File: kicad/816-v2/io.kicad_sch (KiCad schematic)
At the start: 11 parts, among them J2 UART, J3 VIA1 Connector, J4 VIA2 Connector, U10 W65C22NxP, U11 W65C51NxP, U9 W65C22NxP, Y2 1.8342MHz

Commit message: Update KiCad files to get ready for PCB design
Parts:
- removed J3: VIA1 Connector, Connector_PinHeader_2.54mm:PinHeader_2x12_P2.54mm_Vertical, symbol Connector:Conn_01x24_Pin
- added D3, D4: SD103A, Diode_THT:D_DO-35_SOD27_P7.62mm_Horizontal, symbol Device:D_Schottky
- added J10: Mini-DIN-6, custom:TE_5749180-1, symbol Connector:Mini-DIN-6
- added J3: VIA1 Port B, Connector_PinHeader_2.54mm:PinHeader_2x06_P2.54mm_Vertical, symbol Connector:Conn_01x12_Pin
- added J5: PATA, Connector_IDC:IDC-Header_2x20_P2.54mm_Vertical, symbol Connector_Generic:Conn_02x20_Odd_Even
- added J6: PATA_PWR, Connector_PinHeader_2.54mm:PinHeader_1x02_P2.54mm_Vertical, symbol Connector:Conn_01x02_Pin
- added R6, R7: 10K, Resistor_THT:R_Axial_DIN0207_L6.3mm_D2.5mm_P7.62mm_Horizontal, symbol Device:R
- added U6: ATtiny26L-8P, Package_DIP:DIP-20_W7.62mm_Socket, symbol MCU_Microchip_ATtiny:ATtiny26L-8P
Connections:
- net A0: now also J5.35 (Pin_35)
- net A1: now also J5.33 (Pin_33)
- net A2: now also J5.36 (Pin_36)
- net D0: now also J5.17 (Pin_17)
- net D1: now also J5.15 (Pin_15)
- net D2: now also J5.13 (Pin_13)
- net D3: now also J5.11 (Pin_11)
- net D4: now also J5.9 (Pin_9)
- net D5: now also J5.7 (Pin_7)
- net D6: now also J5.5 (Pin_5)
- net D7: now also J5.3 (Pin_3)
- net GND: now also J10.3, J3.10 (Pin_10), J5.19 (Pin_19), J5.2 (Pin_2), J5.22 (Pin_22), J5.24 (Pin_24), J5.26 (Pin_26), J5.30 (Pin_30), J5.40 (Pin_40), J6.2 (Pin_2), U6.16 (GND), U6.6 (GND)
- net RESB: now also J5.1 (Pin_1), U6.10 (~{RESET}/PB7)
- net VCC: now also J10.4, J3.1 (Pin_1), J5.38 (Pin_38), J6.1 (Pin_1), U6.15 (AVCC), U6.5 (VCC)
- net CA1: now reaches U9.40 (CA1)
- net CA1: now also U6.8 (XTAL2/PB5)
- net CA2: now reaches U9.39 (CA2)
- net CA2: now also U6.9 (PB6)
- net at U9.10 (PB0): now also J3.2 (Pin_2)
- net at U9.11 (PB1): now also J3.3 (Pin_3)
- net at U9.12 (PB2): now also J3.4 (Pin_4)
- net at U9.13 (PB3): now also J3.5 (Pin_5)
- net at U9.14 (PB4): now also J3.6 (Pin_6)
- net at U9.15 (PB5): now also J3.7 (Pin_7)
- net at U9.16 (PB6): now also J3.8 (Pin_8)
- net PA0: now reaches U9.2 (PA0)
- net PA0: now also U6.20 (PA0)
- net at U9.17 (PB7): now also J3.9 (Pin_9)
- net at U9.18 (CB1): now also J3.11 (Pin_11)
- net at U9.19 (CB2): now also J3.12 (Pin_12)
- net PA1: now reaches U9.3 (PA1)
- net PA1: now also U6.19 (PA1)
- net PA2: now reaches U9.4 (PA2)
- net PA2: now also U6.18 (PA2)
- net PA3: now reaches U9.5 (PA3)
- net PA3: now also U6.17 (AREF/PA3)
- net PA4: now reaches U9.6 (PA4)
- net PA4: now also U6.14 (PA4)
- net PA5: now reaches U9.7 (PA5)
- net PA5: now also U6.13 (PA5)
- net PA6: now reaches U9.8 (PA6)
- net PA6: now also U6.12 (PA6)
- net PA7: now reaches U9.9 (PA7)
- net PA7: now also U6.11 (PA7)
- net IRQ1: no longer names the net of U9.21 (~{IRQ})
- net IRQ1: now also D4.1 (K)
- net IRQ2: no longer names the net of U10.21 (~{IRQ})
- net IRQ2: now also D3.1 (K)
- new net: J10.5, R6.1
- new net: J10.1, R7.1
- new net IO5CS: J5.37 (Pin_37)
- new net IRQB: D3.2 (A), D4.2 (A)
- new net OE: J5.25 (Pin_25)
- new net PS2CLK: R6.2, U6.4 (PB3)
- new net PS2DATA: R7.2, U6.7 (XTAL1/PB4)
- new net WE: J5.23 (Pin_23)
- no-connect marks 9 -> 31
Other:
- moved on the sheet: RN3

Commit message: Update KiCad files
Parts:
- removed RN3: 10k, Resistor_THT:R_Array_SIP8, symbol Device:R_Network07
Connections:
- net VCC: now also U10.24 (CS1), U11.2 (CS1), U9.24 (CS1)
- net IRQ3: no longer names the net of U11.26 (~{IRQ})
- no-connect marks 31 -> 29

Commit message: Update KiCad files new pcb revision, hopefully working
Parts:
- added C10: 0.1uF, Capacitor_THT:C_Disc_D4.3mm_W1.9mm_P5.00mm, symbol Device:C
- J2: symbol Connector:Conn_01x04_Pin -> Connector_Generic:Conn_01x04
- J3: symbol Connector:Conn_01x12_Pin -> Connector_Generic:Conn_01x12
- J4: symbol Connector:Conn_01x24_Pin -> Connector_Generic:Conn_01x24
- J6: symbol Connector:Conn_01x02_Pin -> Connector_Generic:Conn_01x02
- U10, U9: value W65C22NxP -> W65C22S; symbol PCM_65xx-library:W65C22NxP -> custom:W65C22S
- U11: value W65C51NxP -> W65C51
- U6: value ATtiny26L-8P -> ATtiny26L
- Y2: footprint Package_DIP:DIP-8_W7.62mm_Socket -> Oscillator:Oscillator_DIP-8
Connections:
- net GND: now also C10.2
- net PS2CLK: now also J10.5
- net PS2DATA: now also J10.1
- net VCC: now also R6.1, R7.1, C10.1
- net IO1CS renamed ~{IO1CS}
- net IO2CS renamed ~{IO2CS}
- net IO3CS renamed ~{IO3CS}
- net IO5CS renamed ~{IO5CS}
- net IRQB renamed ~{IRQ}
- net OE renamed ~{OE}
- net RESB renamed ~{RES}
- net RWB renamed R/~{W}
- net WE renamed ~{WE}
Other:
- moved on the sheet: C1, C5, C6, D3, D4, J10, U6

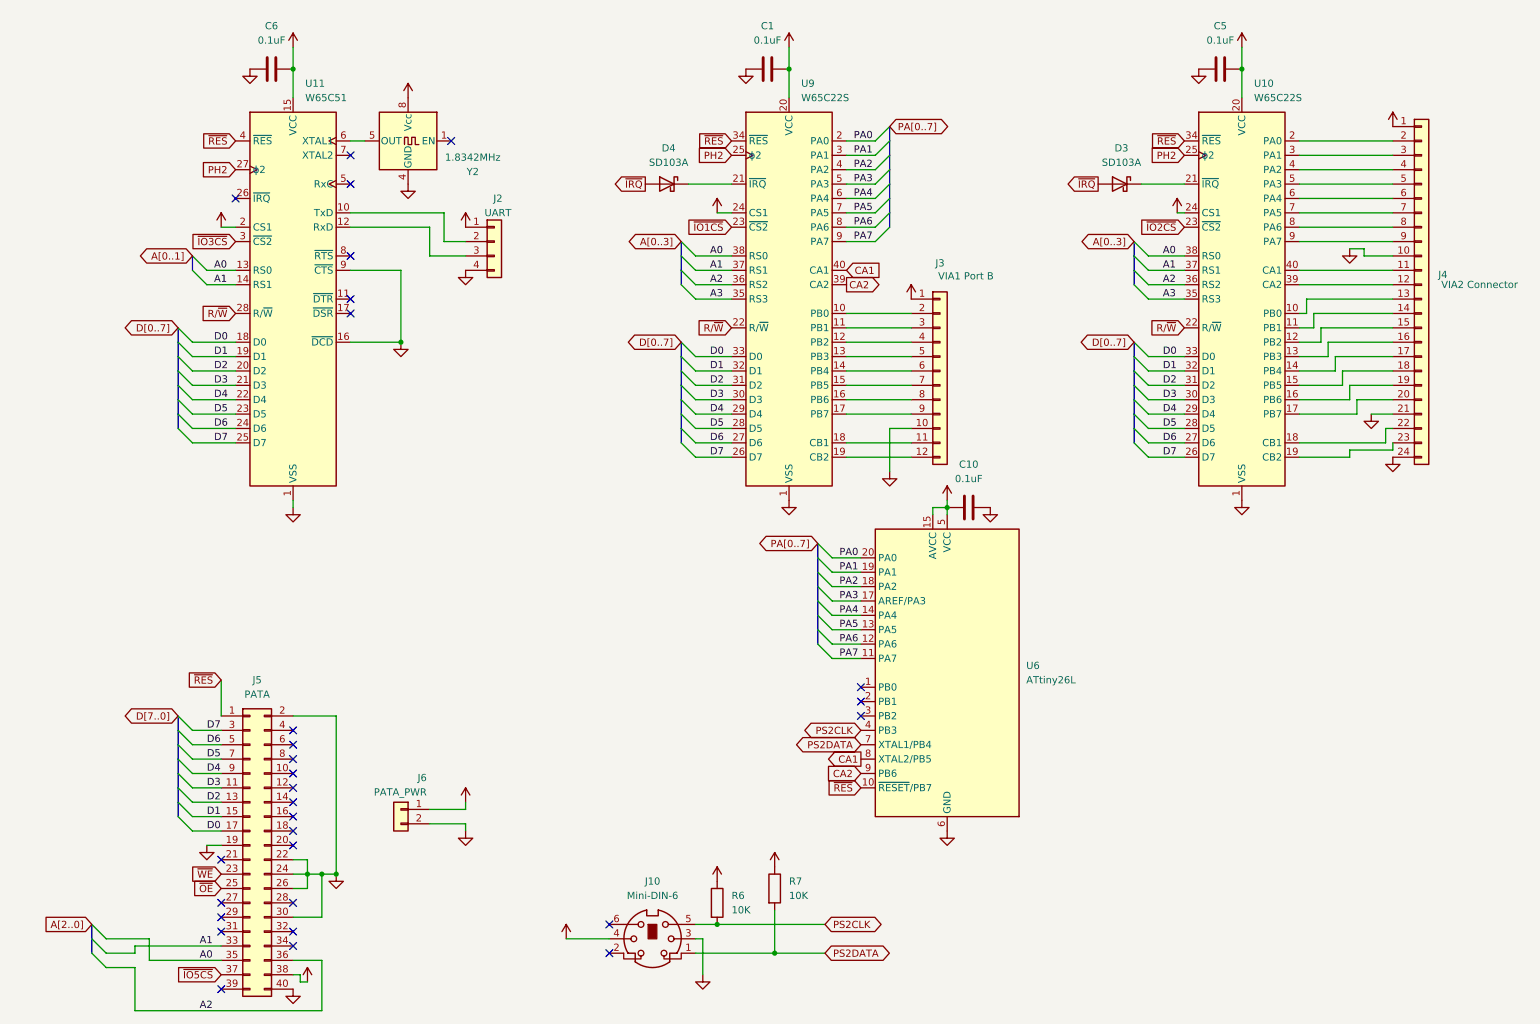
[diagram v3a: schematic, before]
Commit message: Update KiCad files to reflect ROM WE bodge
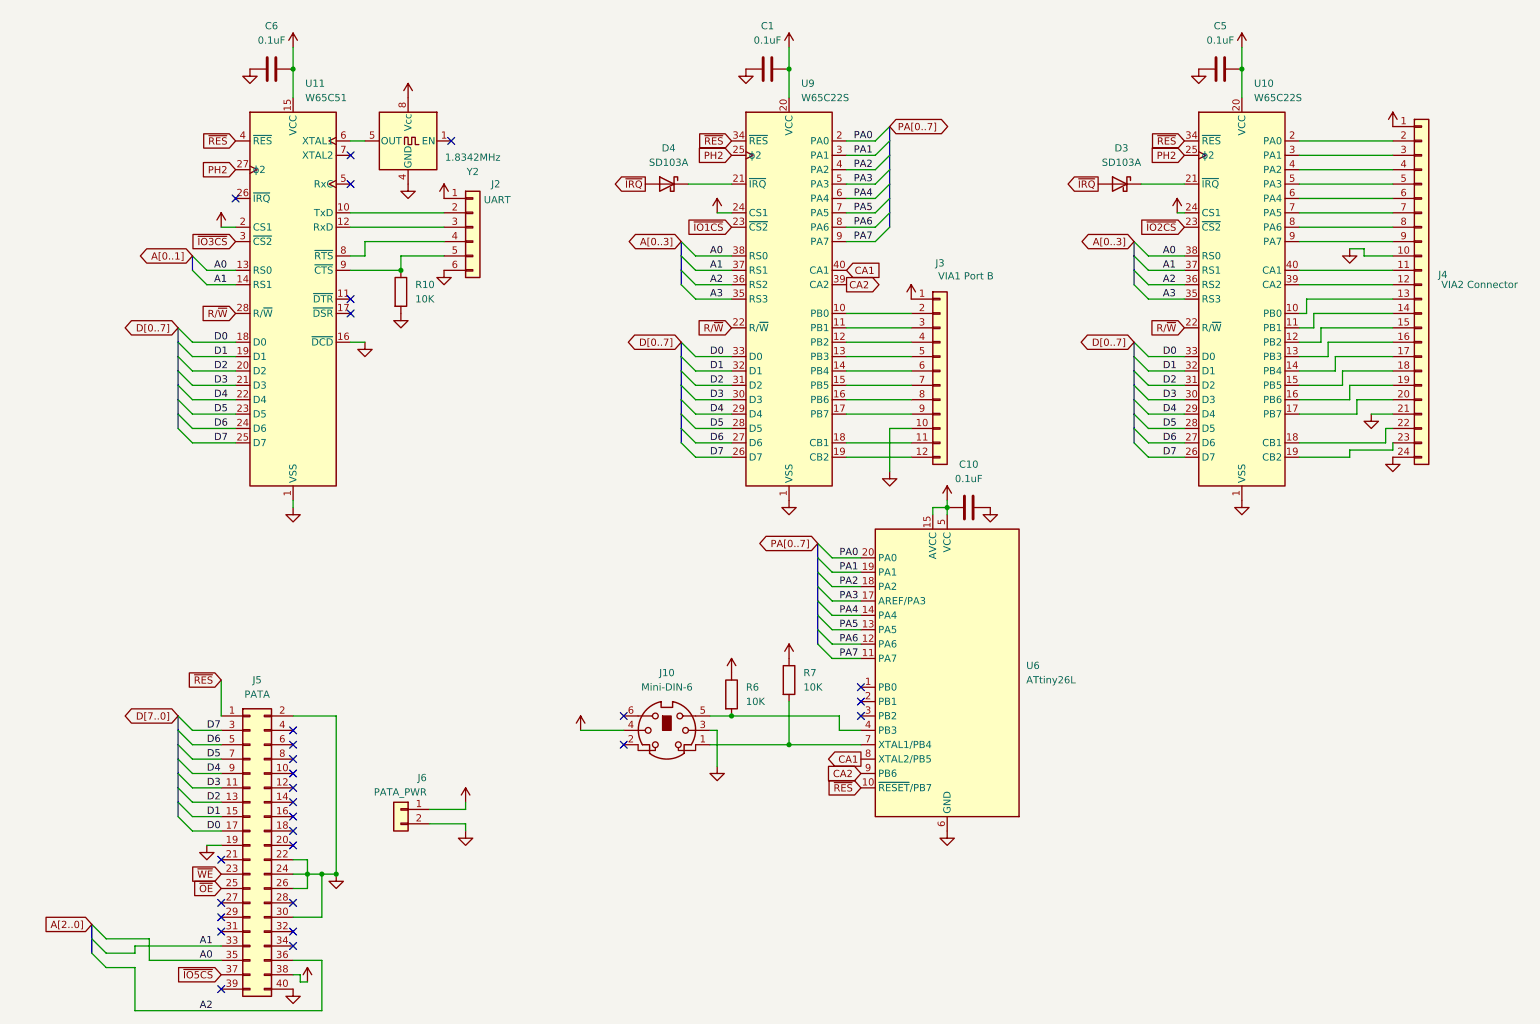
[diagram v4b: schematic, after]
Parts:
- added R10: 10K, Resistor_THT:R_Axial_DIN0207_L6.3mm_D2.5mm_P7.62mm_Horizontal, symbol Device:R
- J2: footprint Connector_PinHeader_2.54mm:PinHeader_1x04_P2.54mm_Vertical -> Connector_PinHeader_2.54mm:PinHeader_1x06_P2.54mm_Vertical; symbol Connector_Generic:Conn_01x04 -> Connector_Generic:Conn_01x06
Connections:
- net GND: now also J2.6 (Pin_6), R10.2; no longer J2.4 (Pin_4), U11.9 (~{CTS})
- net at U11.8 (~{RTS}): now also J2.4 (Pin_4)
- net PS2CLK: no longer names the net of J10.5, R6.2, U6.4 (PB3)
- net PS2DATA: no longer names the net of J10.1, R7.2, U6.7 (XTAL1/PB4)
- new net: J2.5 (Pin_5), R10.1, U11.9 (~{CTS})
- no-connect marks 29 -> 28
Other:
- moved on the sheet: J10, R6, R7
